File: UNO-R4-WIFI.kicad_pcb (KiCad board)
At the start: 4 copper layers, 68.6 x 53.3 mm, 263 parts, among them IC1 NLASB3157DFT2G, IC2 NLASB3157DFT2G, IC3 ISL854102FRZ-T, IC4 SGM2205-3.3XKC3G/TR, J1 TSW-103-07-G-S, J2 SSQ-110-01-G-S, J3 PH2-06-UA, J4 SSQ-108-01-G-S, J5 SSQ-115-01-G-S, J6 SM04B-SRSS-TB(LF)(SN), J7 USB_C_Receptacle_USB2.0_16P, J8 19TW-746, J9 PH2-06-UA, M1 ESP32-S3-MINI-1-N8, P400_SCL1 CMP-018-0004-A.4, P401_SDA1 CMP-018-0004-A.4, Q1 2N7002KT1G, Q2 2N7002KT1G, Q3 2N7002KT1G, SW1 1571636-3, U1 R7FA4M1AB3CFM#AA0, U2 TXB0108DQSR

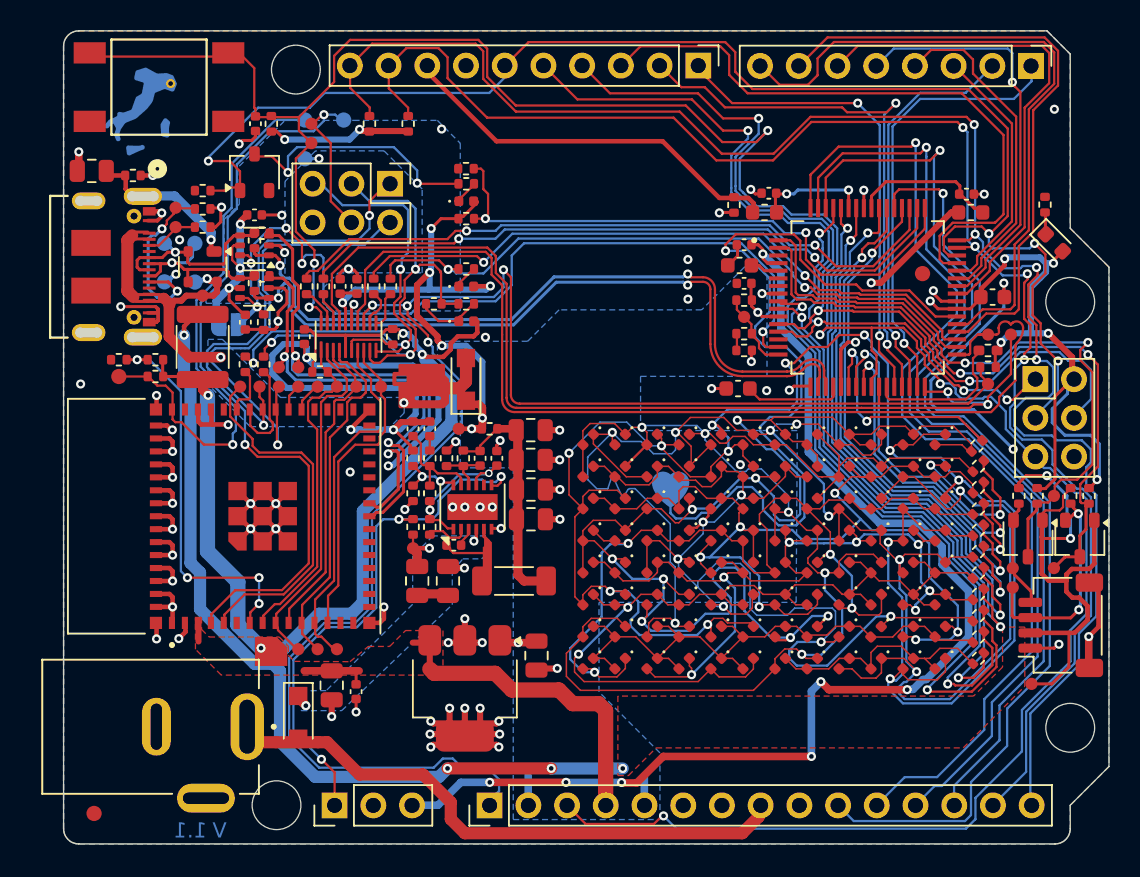
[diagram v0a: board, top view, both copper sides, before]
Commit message: several DRC fixes + dnp components update
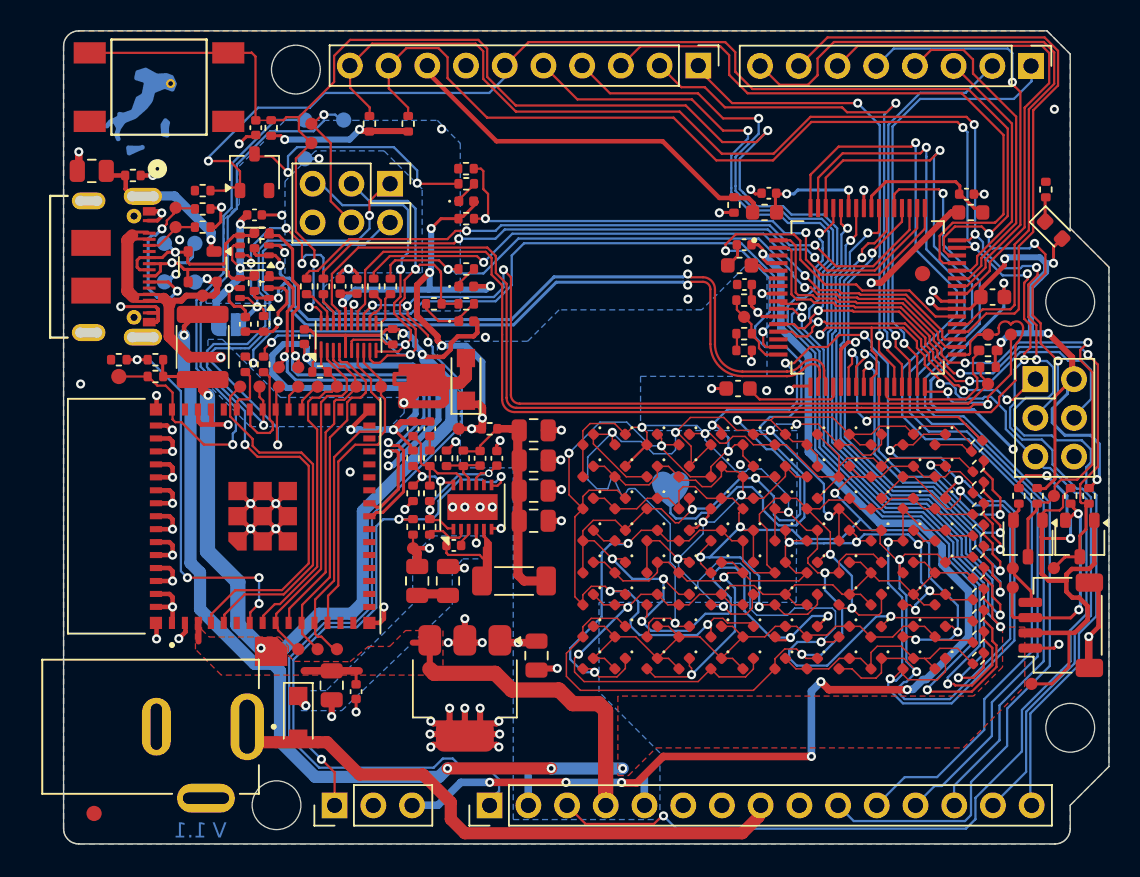
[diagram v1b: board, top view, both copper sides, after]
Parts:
- moved R24 0.99 mm to (178.7, 88.7)
- moved DL3 0.83 mm to (179.2, 91.4)
- moved R3 0.27 mm to (127.8, 84.7)
- moved C1 0.26 mm to (126.8, 84.7)
- moved C15 0.21 mm to (145.1, 110.5)
- moved C17 0.20 mm to (145.1, 106.5)
- moved C18 0.20 mm to (145.1, 104.5)
- moved C16 0.19 mm to (145.1, 108.5)
- moved C29 0.14 mm to (126.1, 97.6)
- moved R1 0.11 mm to (127.3, 97.6)
- moved C3 0.08 mm to (158.9, 95.0)
- turned C10 to -90 degrees
- turned C11 to -90 degrees
- turned F1 to 90 degrees
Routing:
- net +3.3V_I2C: track 35.6 -> 91.3 mm, vias 2 -> 6
- net +3.3V: track 149.1 -> 95.8 mm, vias 10 -> 4
- net VUSB: track 21.9 -> 27.9 mm, vias 2 -> 3
- net +5V: track 132.4 -> 128.9 mm, vias 24 -> 23
- net GND: track 194.1 -> 191.4 mm, vias 82 -> 84
- net /~{RESET}: track 170.3 -> 172.7 mm

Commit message: removed unused footprints + footprints name change + 3D models update
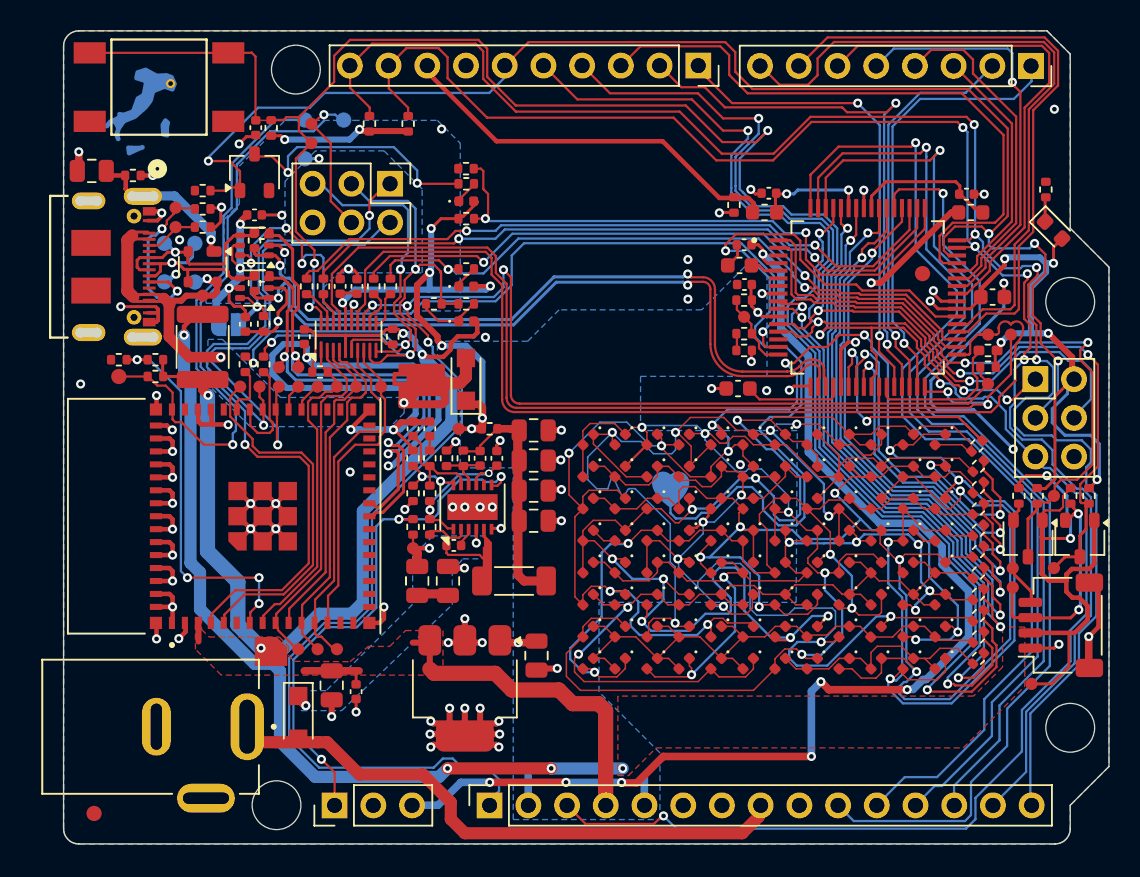
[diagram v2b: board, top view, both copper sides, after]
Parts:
- J2: footprint Connector_PinHeader_2.54mm:PinHeader_1x10_P2.54mm_Vertical -> Connector_PinSocket_2.54mm:PinSocket_1x10_P2.54mm_Vertical
- J4: footprint Connector_PinHeader_2.54mm:PinHeader_1x08_P2.54mm_Vertical -> Connector_PinSocket_2.54mm:PinSocket_1x08_P2.54mm_Vertical
- J5: footprint Connector_PinHeader_2.54mm:PinHeader_1x15_P2.54mm_Vertical -> Connector_PinSocket_2.54mm:PinSocket_1x15_P2.54mm_Vertical
- J7: footprint external_footprints:CON18_1X12_P0_HIR -> external_footprints:CX90B-16P
- J8: footprint external_footprints:MPD_EJ508A -> external_footprints:EJ508A
- SW1: footprint external_footprints:SWITCH_FSM2JSMAA_TYC -> external_footprints:FSM2JSMATR
- U1: footprint external_footprints:QFP50P1200X1200X170-64N -> external_footprints:R7FA4M1AB3CFM#AA0
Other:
- board text removed: "1.1"
- board text removed: "V"

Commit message: BOM update (incomplete)
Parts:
- C10, C13, C15, C16, C17, C18, C19, C28: value CL21A226MAQNNNE -> 22uF
- C11, C12, C25, C26, C29, C3, C30, C7, C8: value GRM155R61H104KE19D -> 100nF
- C14: value GRM1555C1H330JA01D -> 33pF
- C2, C5, C9: value GRM188R61C475KAAJD -> 4.7uF
- C20, C24: value CL05A105KP5NNNC -> 1uF
- C21: value FV21X472K102ECG -> 4.7nF
- C22: value GRM155R71H102KA01D -> 1nF
- C23: value CC0402JRNPO9BN101 -> 100pF
- C6: value CL05A105KP5NNNC -> 1µF
- DL1, DL2, DL4: value KPT-1608YC -> APT1608YC
- F1: value MF-MSMF050-2-W2 -> MF-MSMF050-2
- J6: value SM04B-SRSS-TB(LF)(SN) -> SM04B-SRSS-TB
- R1, R26, R3, R35, R38, R43, R44, R49, R52, R56, R57, R58: value CRCW0402100KFKEDC -> 100k
- R10, R11, R12, R13, R15, R19, R4, R5, R50, R51, R6, R8, R9: value RC0402FR-075K1L -> 5.1k
- R14, R16, R2, R20, R22, R23, R24, R25, R27, R28, R29, R30, R31, R32, R33, R34: value CRCW0402330RJNED -> 330
- R17, R18, R21, R36, R37, R42, R45, R46, R47, R48, R53, R54, R55: value CRCW04020000Z0EDC -> 0
- R39: value CRCW04021M00FKED -> 1M
- R40: value RC0402FR-0713K7L -> 13k
- R41: value AC0402FR-07249KL -> 249k
- R59: value WF04H1003BT -> 100k
- R60: value WF04H1372BTL -> 13k
- R7: value RC0402FR-075K1L -> 5.1k; footprint Resistor_SMD:R_0402_1005Metric_Pad0.72x0.64mm_HandSolder -> Resistor_SMD:R_0402_1005Metric
- SW1: value 1571636-3 -> FSM2JSMATR

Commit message: switched to generic pin headers from Eurocircuits + other BOM improvements
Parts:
- 3V3_IC1, 3V3_TOP1, 5V_TOP1, BUCK_IN_TOP1, CC1, CC2, D+_TOP1, D-_TOP1, ESP_DOWNLOAD_TOP1, ESP_EN_TOP1, ESP_IO1, ESP_IO4, ESP_IO5, ESP_IO6, ESP_IO7, ESP_IO8, ESP_IO9, ESP_MTCK1, ESP_MTDI1, ESP_MTDO1, ESP_MTMS1, EXT_SCL1, EXT_SDA1, MD1, P400_SCL1, P401_SDA1, RES1, SWCLK1, SWDIO1, VCONN_TOP1, VIN_TOP1, uC_VBUS1: value CMP-018-0004-A.4 -> TP-0.8MM
- C6: value 1µF -> 1uF
- D+1, D-1, ESP_DOWNLOAD_BOTTOM1, ESP_EN_BOTTOM1, GND1, GND2, LOVE1, VBUS_CONN1: value CMP-018-0005-A.3 -> TP-1.00MM
- D1, D10, D11, D12, D13, D14, D15, D16, D17, D18, D19, D2, D20, D21, D22, D23, D24, D25, D26, D27, D28, D29, D3, D30, D31, D32, D33, D34, D35, D36, D37, D38, D39, D4, D40, D41, D42, D43, D44, D45, D46, D47, D48, D49, D5, D50, D51, D52, D53, D54, D55, D56, D57, D58, D59, D6, D60, D61, D62, D63, D64, D65, D66, D67, D68, D69, D7, D70, D71, D72, D73, D74, D75, D76, D77, D78, D79, D8, D80, D81, D82, D83, D84, D85, D86, D87, D88, D89, D9, D90, D91, D92, D93, D94, D95, D96: value XHY-STB0603SR -> 150040RS73240
- IC1, IC2: value NLASB3157DFT2G -> 74LVC1G3157DW-7
- J1: value TSW-103-07-G-S -> GPHA-1X03
- J3, J9: value PH2-06-UA -> GPHA-2X03
- J7: value USB_C_Receptacle_USB2.0_16P -> CX90B-16P
- J8: value 19TW-746 -> EJ508A

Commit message: added DRC exclusions
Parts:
- moved J8 0.78 mm to (122.8, 123.6)
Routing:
- net VIN: track 40.6 -> 39.2 mm
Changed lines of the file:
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@@
 			)
 		)
-		(property ki_fp_filters "MountingHole*")
-		(sheetname "Root")
-		(sheetfile "UNO-R4-WIFI.kicad_sch")
 		(attr exclude_from_pos_files exclude_from_bom)
 		(fp_circle
@@
 			)
 		)
-		(property ki_fp_filters "MountingHole*")
-		(sheetname "Root")
-		(sheetfile "UNO-R4-WIFI.kicad_sch")
-		(attr exclude_from_pos_files exclude_from_bom allow_missing_courtyard)
+		(attr exclude_from_pos_files exclude_from_bom)
 		(fp_circle
 			(center 0 0)
@@
 	(footprint "external_footprints:EJ508A"
 		(layer "F.Cu")
-		(at 123.55111 123.98359 -90)
+		(at 122.84361 123.64359 -90)
 		(property "Reference" "J8"
 			(at -0.055 -5.789 90)
@@
 			)
 		)
-		(property ki_fp_filters "MountingHole*")
-		(sheetname "Root")
-		(sheetfile "UNO-R4-WIFI.kicad_sch")
-		(attr exclude_from_pos_files exclude_from_bom allow_missing_courtyard)
+		(attr exclude_from_bom)
 		(fp_circle
 			(center 0 0)
@@
 			(at 0 -1.17 180)
 			(layer "F.SilkS")
+			(hide yes)
 			(effects
 				(font
@@
 			)
 		)
-		(property ki_fp_filters "MountingHole*")
-		(sheetname "Root")
-		(sheetfile "UNO-R4-WIFI.kicad_sch")
-		(attr exclude_from_pos_files exclude_from_bom allow_missing_courtyard)
+		(attr exclude_from_bom)
 		(fp_circle
 			(center 0 0)
@@
 	)
 	(segment
-		(start 131.5061 125.0026)
-		(end 133.62297 127.11948)
-		(width 0.8)
-		(layer "F.Cu")
-		(net 17)
-	)
-	(segment
-		(start 137.78907 127.11948)
-		(end 139.6111 128.9415)
-		(width 0.8)
-		(layer "F.Cu")
-		(net 17)
-	)
-	(segment
 		(start 159.81201 129.89344)
 		(end 159.81201 129.25269)
@@
 	)
 	(segment
-		(start 126.1011 124.40917)
-		(end 126.1011 123.3676)
-		(width 0.8)
-		(layer "F.Cu")
-		(net 17)
-	)
-	(segment
-		(start 139.6111 130.0477)
-		(end 139.6111 128.9415)
-		(width 0.8)
-		(layer "F.Cu")
-		(net 17)
-	)
-	(segment
-		(start 133.62297 127.11948)
-		(end 137.78907 127.11948)
+		(start 140.53701 130.97361)
+		(end 158.73183 130.97361)
 		(width 0.8)
 		(layer "F.Cu")
@@
 	)
 	(segment
-		(start 158.73183 130.97361)
-		(end 159.81201 129.89344)
+		(start 159.81201 129.25269)
+		(end 159.9311 129.1336)
 		(width 0.8)
 		(layer "F.Cu")
@@
 	)
 	(segment
-		(start 126.69453 125.0026)
-		(end 129.6061 125.0026)
+		(start 139.6111 128.9415)
+		(end 139.6111 130.0477)
 		(width 0.8)
 		(layer "F.Cu")
@@
 	)
 	(segment
-		(start 159.81201 129.25269)
-		(end 159.9311 129.1336)
+		(start 139.6111 130.0477)
+		(end 140.53701 130.97361)
 		(width 0.8)
 		(layer "F.Cu")
@@
 	)
 	(segment
-		(start 140.53701 130.97361)
-		(end 158.73183 130.97361)
+		(start 125.54861 123.64359)
+		(end 126.90762 125.0026)
 		(width 0.8)
 		(layer "F.Cu")
@@
 	)
 	(segment
-		(start 129.6061 125.0026)
-		(end 130.9061 125.0026)
+		(start 131.5061 125.0026)
+		(end 133.62297 127.11948)
 		(width 0.8)
 		(layer "F.Cu")
@@
 	)
 	(segment
-		(start 130.9061 125.0026)
+		(start 126.90762 125.0026)
 		(end 131.5061 125.0026)
 		(width 0.8)
@@
 	)
 	(segment
-		(start 126.1011 124.40917)
-		(end 126.69453 125.0026)
+		(start 133.62297 127.11948)
+		(end 137.78907 127.11948)
 		(width 0.8)
 		(layer "F.Cu")
@@
 	)
 	(segment
-		(start 139.6111 130.0477)
-		(end 140.53701 130.97361)
+		(start 158.73183 130.97361)
+		(end 159.81201 129.89344)
 		(width 0.8)
 		(layer "F.Cu")
@@
 	)
 	(segment
-		(start 126.1011 124.15262)
-		(end 126.9511 125.00261)
+		(start 137.78907 127.11948)
+		(end 139.6111 128.9415)
 		(width 0.8)
 		(layer "F.Cu")
